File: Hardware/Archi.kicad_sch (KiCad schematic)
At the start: 10 parts, among them J3 Alimentación, J4 Analógico, J5 Digital/PWM, J6 Digital/PWM, U2 RESET

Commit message: Cambio todos los conectores a SMD
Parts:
- J3, J4, J5, J6: now not fitted
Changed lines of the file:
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@@
 		(in_bom yes)
 		(on_board yes)
-		(dnp no)
+		(dnp yes)
 		(property "Reference" "J3"
 			(at 58.42 52.07 0)
@@
 		(in_bom yes)
 		(on_board yes)
-		(dnp no)
+		(dnp yes)
 		(property "Reference" "J5"
 			(at 68.58 46.99 0)
@@
 		(in_bom yes)
 		(on_board yes)
-		(dnp no)
+		(dnp yes)
 		(property "Reference" "J4"
 			(at 58.42 80.01 0)
@@
 		(in_bom yes)
 		(on_board yes)
-		(dnp no)
+		(dnp yes)
 		(property "Reference" "J6"
 			(at 68.58 80.01 0)

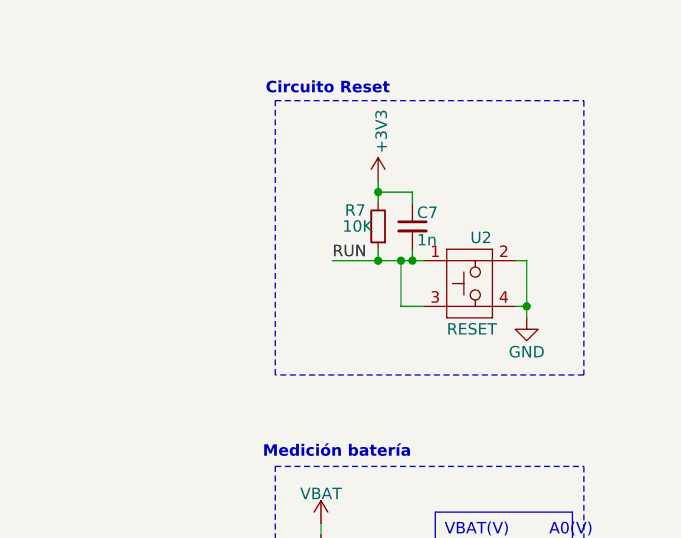
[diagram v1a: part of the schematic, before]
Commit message: Modifico error del botón en sch y ruteo pistas de potencia
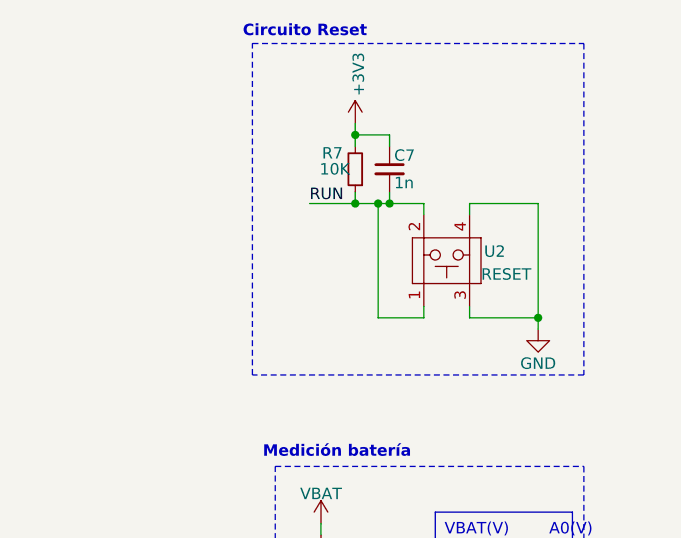
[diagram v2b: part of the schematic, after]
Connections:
- net GND: now also U2.3; no longer U2.2
- net RUN: now also U2.2; no longer U2.3
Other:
- moved on the sheet: C7, R7, U2

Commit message: Correcciones en el ruteo, agrego fiduciales, 3D y serigrafía
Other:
- company: (none) -> Newsan
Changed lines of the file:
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@@
 	(title_block
 		(title "Archi Bot")
-		(date "2024-07-18")
-		(rev "1.1")
+		(date "2024-09-27")
+		(rev "1.2")
+		(company "Newsan")
 	)
 	(junction

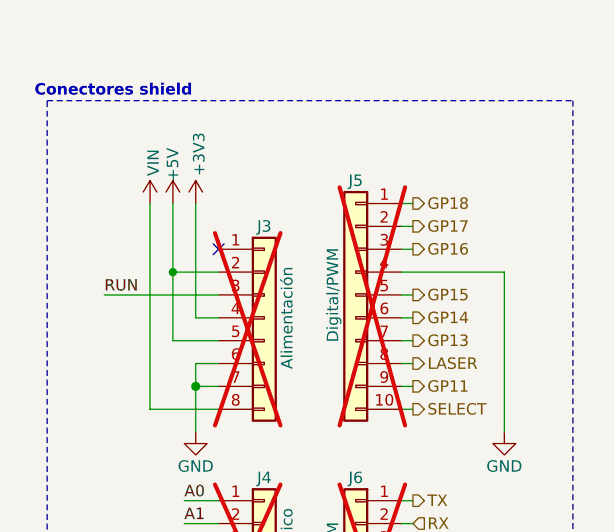
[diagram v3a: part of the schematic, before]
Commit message: Agrego test points, cambio conectores, finalizo v1.2
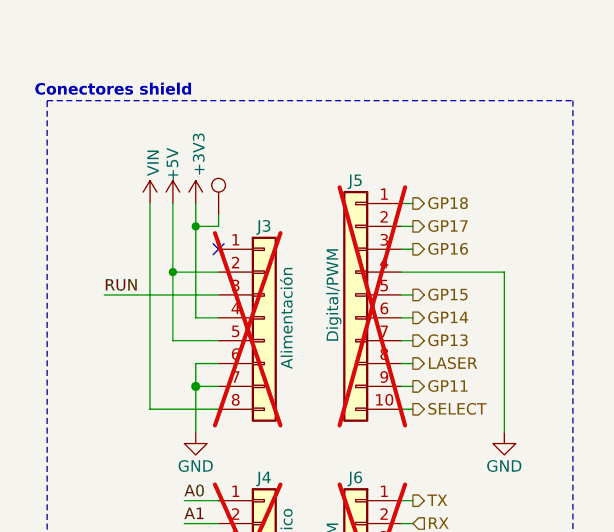
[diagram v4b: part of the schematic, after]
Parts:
- added TP29: TestPoint, TestPoint:TestPoint_Pad_D1.0mm, symbol Connector:TestPoint
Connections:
- net +3V3: now also TP29.1
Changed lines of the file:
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@@
+	)
+	(junction
+		(at 50.8 52.07)
+		(diameter 0)
+		(color 0 0 0 0)
 	)
 	(junction
@@
 	(wire
 		(pts
+			(xy 50.8 52.07) (xy 50.8 62.23)
+		)
+		(stroke
+			(width 0)
+			(type solid)
+		)
+	)
+	(wire
+		(pts
 			(xy 146.05 62.23) (xy 146.05 60.96)
 		)
@@
 	(wire
 		(pts
-			(xy 50.8 49.53) (xy 50.8 62.23)
+			(xy 50.8 49.53) (xy 50.8 52.07)
 		)
 		(stroke
@@
 	(wire
 		(pts
+			(xy 53.34 50.8) (xy 53.34 52.07)
+		)
+		(stroke
+			(width 0)
+			(type default)
+		)
+	)
+	(wire
+		(pts
 			(xy 52.07 90.17) (xy 53.34 90.17)
 		)
@@
 		(pts
 			(xy 73.66 90.17) (xy 74.93 90.17)
+		)
+		(stroke
+			(width 0)
+			(type default)
+		)
+	)
+	(wire
+		(pts
+			(xy 53.34 52.07) (xy 50.8 52.07)
 		)
 		(stroke
@@
 					(unit 1)
 				)
+			)
+		)
+	)
+	(symbol
+		(lib_id "Connector:TestPoint")
+		(at 53.34 50.8 0)
+		(unit 1)
+		(exclude_from_sim no)
+		(in_bom yes)
+		(on_board yes)
+		(dnp no)
+		(fields_autoplaced yes)
+		(property "Reference" "TP29"
+			(at 55.88 46.2279 0)
+			(effects
+				(font
+					(size 1.27 1.27)
+				)
+				(justify left)
+				(hide yes)
+			)
+		)
+		(property "Value" "TestPoint"
+			(at 55.88 48.7679 0)
+			(effects
+				(font
+					(size 1.27 1.27)
+				)
+				(justify left)
+				(hide yes)
+			)
+		)
+		(property "Footprint" "TestPoint:TestPoint_Pad_D1.0mm"
+			(at 58.42 50.8 0)
+			(effects
+				(font
+					(size 1.27 1.27)
+				)
+				(hide yes)
+			)
+		)
+		(property "Datasheet" "~"
+			(at 58.42 50.8 0)
+			(effects
+				(font
+					(size 1.27 1.27)
+				)
+				(hide yes)
+			)
+		)
+		(property "Description" "test point"
+			(at 53.34 50.8 0)
+			(effects
+				(font
+					(size 1.27 1.27)
+				)
+				(hide yes)
+			)
+		)
+		(pin "1"
+		)
+		(instances
+			(project "ArchiBot"
+				(path "/e63e39d7-6ac0-4ffd-8aa3-1841a4541b55/b884adbc-a8b2-4c02-abce-5cda7e46c7c7"
+					(reference "TP29")
+					(unit 1)
+				)

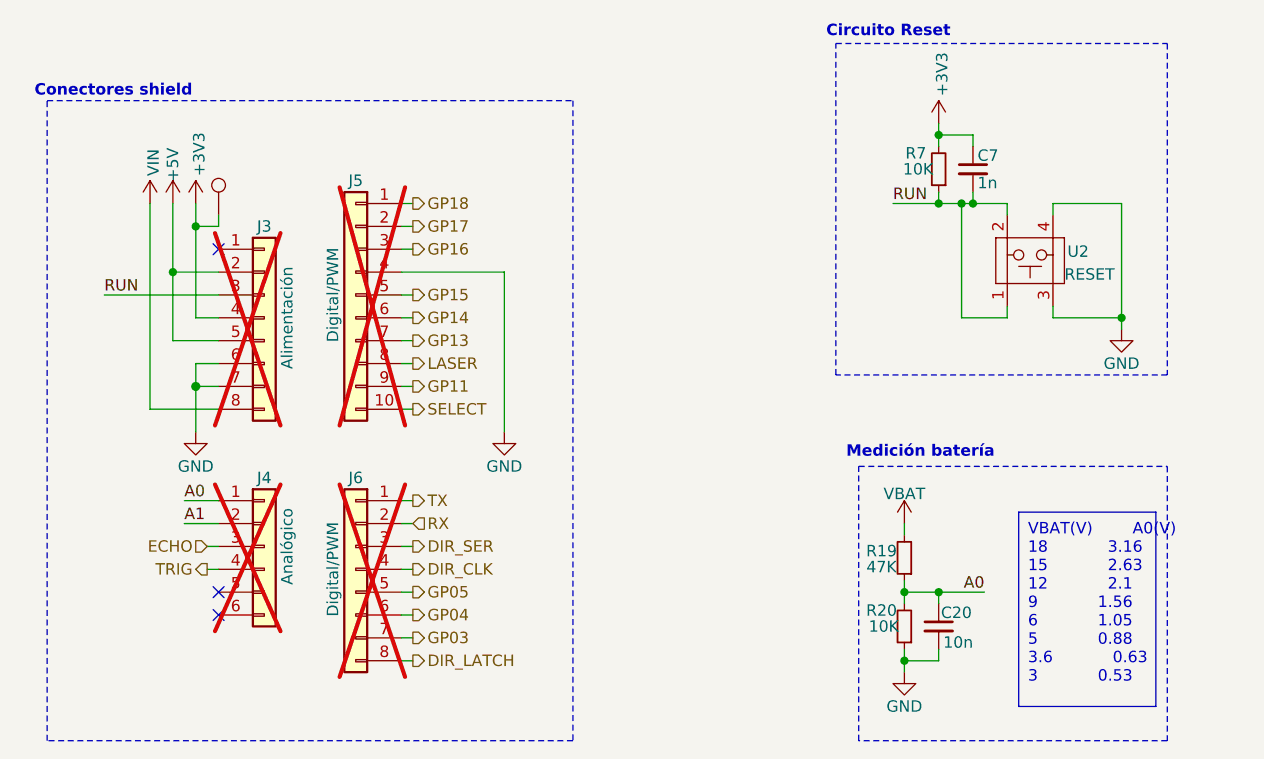
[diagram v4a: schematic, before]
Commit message: Agrego testpoints y modifico footprint de bornera
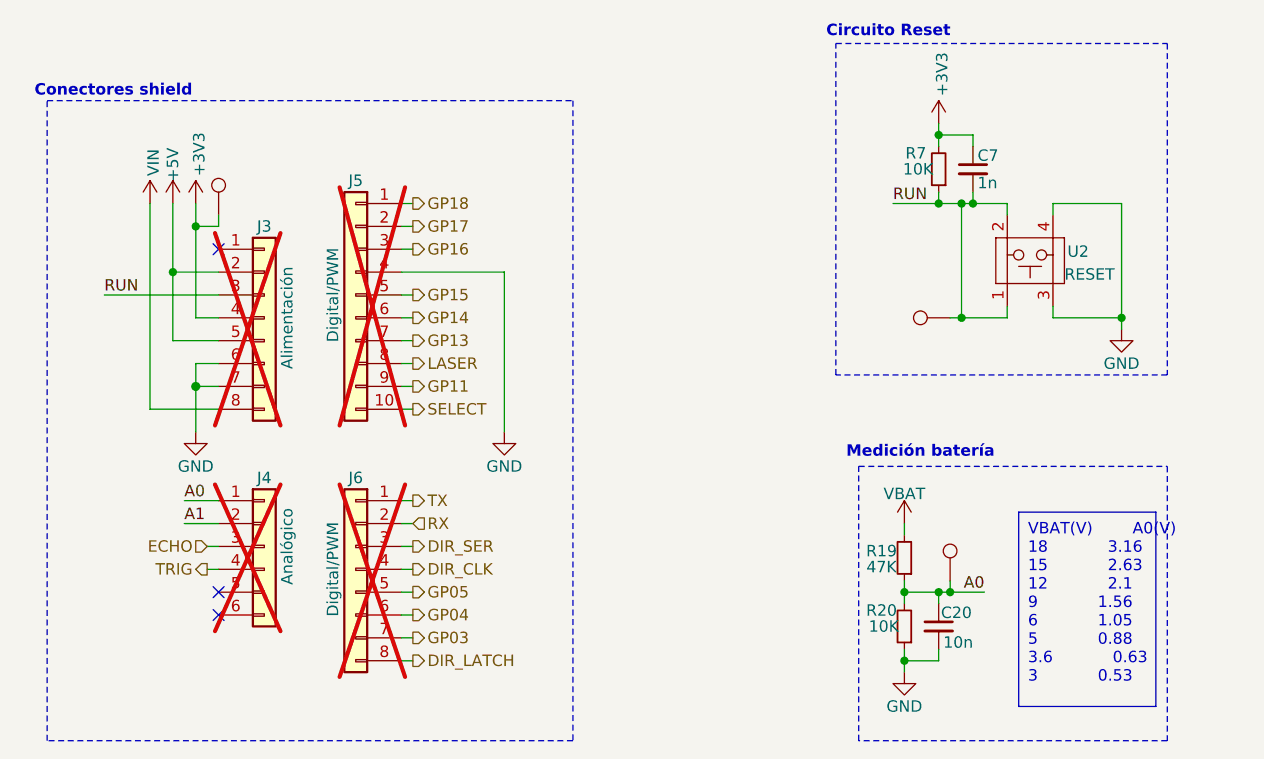
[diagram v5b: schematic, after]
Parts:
- added TP4, TP5: TestPoint, TestPoint:TestPoint_Pad_D1.0mm, symbol Connector:TestPoint
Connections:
- net A0: now also TP5.1
- net RUN: now also TP4.1
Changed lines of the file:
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@@
+	)
+	(junction
+		(at 134.62 92.71)
+		(diameter 0)
+		(color 0 0 0 0)
+	)
+	(junction
+		(at 135.89 62.23)
+		(diameter 0)
+		(color 0 0 0 0)
 	)
 	(junction
@@
 	(wire
 		(pts
+			(xy 134.62 62.23) (xy 135.89 62.23)
+		)
+		(stroke
+			(width 0)
+			(type default)
+		)
+	)
+	(wire
+		(pts
 			(xy 53.34 69.85) (xy 50.8 69.85)
 		)
@@
 	(wire
 		(pts
-			(xy 133.35 92.71) (xy 138.43 92.71)
+			(xy 133.35 92.71) (xy 134.62 92.71)
 		)
 		(stroke
@@
 	(wire
 		(pts
+			(xy 134.62 92.71) (xy 138.43 92.71)
+		)
+		(stroke
+			(width 0)
+			(type default)
+		)
+	)
+	(wire
+		(pts
 			(xy 129.54 92.71) (xy 129.54 93.98)
 		)
@@
 		(pts
 			(xy 133.35 49.53) (xy 135.89 49.53)
+		)
+		(stroke
+			(width 0)
+			(type default)
+		)
+	)
+	(wire
+		(pts
+			(xy 134.62 91.44) (xy 134.62 92.71)
 		)
 		(stroke
@@
 				(path "/e63e39d7-6ac0-4ffd-8aa3-1841a4541b55/b884adbc-a8b2-4c02-abce-5cda7e46c7c7"
 					(reference "J3")
+					(unit 1)
+				)
+			)
+		)
+	)
+	(symbol
+		(lib_id "Connector:TestPoint")
+		(at 134.62 62.23 90)
+		(unit 1)
+		(exclude_from_sim no)
+		(in_bom yes)
+		(on_board yes)
+		(dnp no)
+		(fields_autoplaced yes)
+		(property "Reference" "TP4"
+			(at 130.0479 59.69 0)
+			(effects
+				(font
+					(size 1.27 1.27)
+				)
+				(justify left)
+				(hide yes)
+			)
+		)
+		(property "Value" "TestPoint"
+			(at 132.5879 59.69 0)
+			(effects
+				(font
+					(size 1.27 1.27)
+				)
+				(justify left)
+				(hide yes)
+			)
+		)
+		(property "Footprint" "TestPoint:TestPoint_Pad_D1.0mm"
+			(at 134.62 57.15 0)
+			(effects
+				(font
+					(size 1.27 1.27)
+				)
+				(hide yes)
+			)
+		)
+		(property "Datasheet" "~"
+			(at 134.62 57.15 0)
+			(effects
+				(font
+					(size 1.27 1.27)
+				)
+				(hide yes)
+			)
+		)
+		(property "Description" "test point"
+			(at 134.62 62.23 0)
+			(effects
+				(font
+					(size 1.27 1.27)
+				)
+				(hide yes)
+			)
+		)
+		(pin "1"
+		)
+		(instances
+			(project "ArchiBot"
+				(path "/e63e39d7-6ac0-4ffd-8aa3-1841a4541b55/b884adbc-a8b2-4c02-abce-5cda7e46c7c7"
+					(reference "TP4")
 					(unit 1)
 				)
@@
 					(unit 1)
 				)
+			)
+		)
+	)
+	(symbol
+		(lib_id "Connector:TestPoint")
+		(at 134.62 91.44 0)
+		(unit 1)
+		(exclude_from_sim no)
+		(in_bom yes)
+		(on_board yes)
+		(dnp no)
+		(fields_autoplaced yes)
+		(property "Reference" "TP5"
+			(at 137.16 86.8679 0)
+			(effects
+				(font
+					(size 1.27 1.27)
+				)
+				(justify left)
+				(hide yes)
+			)
+		)
+		(property "Value" "TestPoint"
+			(at 137.16 89.4079 0)
+			(effects
+				(font
+					(size 1.27 1.27)
+				)
+				(justify left)
+				(hide yes)
+			)
+		)
+		(property "Footprint" "TestPoint:TestPoint_Pad_D1.0mm"
+			(at 139.7 91.44 0)
+			(effects
+				(font
+					(size 1.27 1.27)
+				)
+				(hide yes)
+			)
+		)
+		(property "Datasheet" "~"
+			(at 139.7 91.44 0)
+			(effects
+				(font
+					(size 1.27 1.27)
+				)
+				(hide yes)
+			)
+		)
+		(property "Description" "test point"
+			(at 134.62 91.44 0)
+			(effects
+				(font
+					(size 1.27 1.27)
+				)
+				(hide yes)
+			)
+		)
+		(pin "1"
+		)
+		(instances
+			(project "ArchiBot"
+				(path "/e63e39d7-6ac0-4ffd-8aa3-1841a4541b55/b884adbc-a8b2-4c02-abce-5cda7e46c7c7"
+					(reference "TP5")
+					(unit 1)
+				)

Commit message: Actualizo campo descripción
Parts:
- J3, J6: PartNumber (none) -> PH1-08-UA; PurchaseLink (none) -> https://www.digikey.com/en/products/detail/adam-tech/PH1-08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
- J4: PartNumber (none) -> PH1-06-UA; PurchaseLink (none) -> https://www.digikey.com/en/products/detail/adam-tech/PH1-06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
- J5: PartNumber (none) -> PH1-10-UA; PurchaseLink (none) -> https://www.digikey.com/en/products/detail/adam-tech/ph1-10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
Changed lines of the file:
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@@
 			)
 		)
-		(property "Description" "Unpolarized capacitor, small symbol"
+		(property "Description" "CAP CER 1000PF 50V C0G/NP0 0603"
 			(at 137.16 45.72 0)
 			(effects
@@
 			)
 		)
-		(property "Description" "Resistor, small symbol"
+		(property "Description" "RES 47K OHM 1% 1/10W 0603"
 			(at 129.54 88.9 0)
 			(effects
@@
 			)
 		)
-		(property "Description" ""
+		(property "Description" "CONN HEADER VERT 8POS 2.54MM"
 			(at 58.42 62.23 0)
 			(effects
@@
 			)
 		)
-		(property "PartNumber" ""
+		(property "PartNumber" "PH1-08-UA"
 			(at 58.42 62.23 0)
 			(effects
@@
 			)
 		)
-		(property "PurchaseLink" ""
+		(property "PurchaseLink" "https://www.digikey.com/en/products/detail/adam-tech/PH1-08-UA/9830442"
 			(at 58.42 62.23 0)
 			(effects
@@
 			)
 		)
-		(property "Description" ""
+		(property "Description" "CONN HEADER VERT 10POS 2.54MM"
 			(at 68.58 59.69 0)
 			(effects
@@
 			)
 		)
-		(property "PartNumber" ""
+		(property "PartNumber" "PH1-10-UA"
 			(at 68.58 59.69 0)
 			(effects
@@
 			)
 		)
-		(property "PurchaseLink" ""
+		(property "PurchaseLink" "https://www.digikey.com/en/products/detail/adam-tech/ph1-10-ua/9830653"
 			(at 68.58 59.69 0)
 			(effects
@@
 			)
 		)
-		(property "Description" "PTS645SM43SMTR92LFS"
+		(property "Description" "SWITCH TACTILE SPST-NO 0.05A 12V"
 			(at 139.7 60.96 0)
 			(effects
@@
 			)
 		)
-		(property "Description" ""
+		(property "Description" "CONN HEADER VERT 6POS 2.54MM"
 			(at 58.42 87.63 0)
 			(effects
@@
 			)
 		)
-		(property "PartNumber" ""
+		(property "PartNumber" "PH1-06-UA"
 			(at 58.42 87.63 0)
 			(effects
@@
 			)
 		)
-		(property "PurchaseLink" ""
+		(property "PurchaseLink" "https://www.digikey.com/en/products/detail/adam-tech/PH1-06-UA/9830394"
 			(at 58.42 87.63 0)
 			(effects
@@
 			)
 		)
-		(property "Description" "Resistor, small symbol"
+		(property "Description" "RES 10K OHM 1% 1/10W 0603"
 			(at 133.35 45.72 0)
 			(effects
@@
 			)
 		)
-		(property "Description" "Unpolarized capacitor, small symbol"
+		(property "Description" "CAP CER 10000PF 100V X7R 0603"
 			(at 133.35 96.52 0)
 			(effects
@@
 			)
 		)
-		(property "Description" ""
+		(property "Description" "CONN HEADER VERT 8POS 2.54MM"
 			(at 68.58 90.17 0)
 			(effects
@@
 			)
 		)
-		(property "PartNumber" ""
+		(property "PartNumber" "PH1-08-UA"
 			(at 68.58 90.17 0)
 			(effects
@@
 			)
 		)
-		(property "PurchaseLink" ""
+		(property "PurchaseLink" "https://www.digikey.com/en/products/detail/adam-tech/PH1-08-UA/9830442"
 			(at 68.58 90.17 0)
 			(effects
@@
 			)
 		)
-		(property "Description" "Resistor, small symbol"
+		(property "Description" "RES 10K OHM 1% 1/10W 0603"
 			(at 129.54 96.52 0)
 			(effects

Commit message: Agrego campos manufacturer y package
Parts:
- C20, C7: Manufacturer (none) -> Murata Electronics; Package (none) -> 0603 (1608 Metric)
- J3, J6: Manufacturer (none) -> Adam Tech; Package (none) -> 8POS 0.100" (2.54mm)
- J4: Manufacturer (none) -> Adam Tech; Package (none) -> 6POS 0.100" (2.54mm)
- J5: Manufacturer (none) -> Adam Tech; Package (none) -> 10POS 0.100" (2.54mm)
- R19, R20, R7: Manufacturer (none) -> YAGEO; Package (none) -> 0603 (1608 Metric)
- U2: Manufacturer (none) -> C&K; Package (none) -> Gull Wing 6.00mm x 6.00mm; PartNumber PTS645SM43SMTR92LFS -> PTS645SM43SMTR92 LFS
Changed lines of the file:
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@@
+			)
+		)
+		(property "Manufacturer" "Murata Electronics"
+			(at 137.16 45.72 0)
+			(effects
+				(font
+					(size 1.27 1.27)
+				)
+				(hide yes)
+			)
+		)
+		(property "Package" "0603 (1608 Metric)"
+			(at 137.16 45.72 0)
+			(effects
+				(font
+					(size 1.27 1.27)
+				)
+				(hide yes)
 			)
 		)
@@
 			)
 		)
+		(property "Manufacturer" "YAGEO"
+			(at 129.54 88.9 0)
+			(effects
+				(font
+					(size 1.27 1.27)
+				)
+				(hide yes)
+			)
+		)
+		(property "Package" "0603 (1608 Metric)"
+			(at 129.54 88.9 0)
+			(effects
+				(font
+					(size 1.27 1.27)
+				)
+				(hide yes)
+			)
+		)
 		(pin "2"
 		)
@@
 		)
 		(property "PurchaseLink" "https://www.digikey.com/en/products/detail/adam-tech/PH1-08-UA/9830442"
+			(at 58.42 62.23 0)
+			(effects
+				(font
+					(size 1.27 1.27)
+				)
+				(hide yes)
+			)
+		)
+		(property "Manufacturer" "Adam Tech"
+			(at 58.42 62.23 0)
+			(effects
+				(font
+					(size 1.27 1.27)
+				)
+				(hide yes)
+			)
+		)
+		(property "Package" "8POS 0.100\" (2.54mm)"
 			(at 58.42 62.23 0)
 			(effects
@@
 			)
 		)
+		(property "Manufacturer" ""
+			(at 134.62 62.23 0)
+			(effects
+				(font
+					(size 1.27 1.27)
+				)
+				(hide yes)
+			)
+		)
+		(property "Package" ""
+			(at 134.62 62.23 0)
+			(effects
+				(font
+					(size 1.27 1.27)
+				)
+				(hide yes)
+			)
+		)
 		(pin "1"
 		)
@@
 		)
 		(property "PurchaseLink" "https://www.digikey.com/en/products/detail/adam-tech/ph1-10-ua/9830653"
+			(at 68.58 59.69 0)
+			(effects
+				(font
+					(size 1.27 1.27)
+				)
+				(hide yes)
+			)
+		)
+		(property "Manufacturer" "Adam Tech"
+			(at 68.58 59.69 0)
+			(effects
+				(font
+					(size 1.27 1.27)
+				)
+				(hide yes)
+			)
+		)
+		(property "Package" "10POS 0.100\" (2.54mm)"
 			(at 68.58 59.69 0)
 			(effects
@@
 			)
 		)
+		(property "Manufacturer" ""
+			(at 53.34 50.8 0)
+			(effects
+				(font
+					(size 1.27 1.27)
+				)
+				(hide yes)
+			)
+		)
+		(property "Package" ""
+			(at 53.34 50.8 0)
+			(effects
+				(font
+					(size 1.27 1.27)
+				)
+				(hide yes)
+			)
+		)
 		(pin "1"
 		)
@@
 			)
 		)
-		(property "PartNumber" "PTS645SM43SMTR92LFS"
+		(property "PartNumber" "PTS645SM43SMTR92 LFS"
 			(at 140.97 60.96 0)
 			(effects
@@
 		)
 		(property "PurchaseLink" "https://www.digikey.com/short/0bzh950w"
+			(at 140.97 60.96 0)
+			(effects
+				(font
+					(size 1.27 1.27)
+				)
+				(hide yes)
+			)
+		)
+		(property "Manufacturer" "C&K"
+			(at 140.97 60.96 0)
+			(effects
+				(font
+					(size 1.27 1.27)
+				)
+				(hide yes)
+			)
+		)
+		(property "Package" "Gull Wing 6.00mm x 6.00mm "
 			(at 140.97 60.96 0)
 			(effects
@@
 			)
 		)
+		(property "Manufacturer" "Adam Tech"
+			(at 58.42 87.63 0)
+			(effects
+				(font
+					(size 1.27 1.27)
+				)
+				(hide yes)
+			)
+		)
+		(property "Package" "6POS 0.100\" (2.54mm)"
+			(at 58.42 87.63 0)
+			(effects
+				(font
+					(size 1.27 1.27)
+				)
+				(hide yes)
+			)
+		)
 		(pin "1"
 		)
@@
 			)
 		)
+		(property "Manufacturer" "YAGEO"
+			(at 133.35 45.72 0)
+			(effects
+				(font
+					(size 1.27 1.27)
+				)
+				(hide yes)
+			)
+		)
+		(property "Package" "0603 (1608 Metric)"
+			(at 133.35 45.72 0)
+			(effects
+				(font
+					(size 1.27 1.27)
+				)
+				(hide yes)
+			)
+		)
 		(pin "2"
 		)
@@
 			)
 		)
+		(property "Manufacturer" "Murata Electronics"
+			(at 133.35 96.52 0)
+			(effects
+				(font
+					(size 1.27 1.27)
+				)
+				(hide yes)
+			)
+		)
+		(property "Package" "0603 (1608 Metric)"
+			(at 133.35 96.52 0)
+			(effects
+				(font
+					(size 1.27 1.27)
+				)
+				(hide yes)
+			)
+		)
 		(pin "1"
 		)
@@
 		)
 		(property "PurchaseLink" "https://www.digikey.com/en/products/detail/adam-tech/PH1-08-UA/9830442"
+			(at 68.58 90.17 0)
+			(effects
+				(font
+					(size 1.27 1.27)
+				)
+				(hide yes)
+			)
+		)
+		(property "Manufacturer" "Adam Tech"
+			(at 68.58 90.17 0)
+			(effects
+				(font
+					(size 1.27 1.27)
+				)
+				(hide yes)
+			)
+		)
+		(property "Package" "8POS 0.100\" (2.54mm)"
 			(at 68.58 90.17 0)
 			(effects
@@
 			)
 		)
+		(property "Manufacturer" ""
+			(at 134.62 91.44 0)
+			(effects
+				(font
+					(size 1.27 1.27)
+				)
+				(hide yes)
+			)
+		)
+		(property "Package" ""
+			(at 134.62 91.44 0)
+			(effects
+				(font
+					(size 1.27 1.27)
+				)
+				(hide yes)
+			)
+		)
 		(pin "1"
 		)
@@
 			(at 129.54 96.52 0)
 			(effects
+				(font
+					(size 1.27 1.27)
+				)
+				(hide yes)
+			)
+		)
+		(property "Manufacturer" "YAGEO"
+			(at 129.54 96.52 0)
+			(effects
+				(font
+					(size 1.27 1.27)
+				)
+				(hide yes)
+			)
+		)
+		(property "Package" "0603 (1608 Metric)"
+			(at 129.54 96.52 0)
+			(effects
